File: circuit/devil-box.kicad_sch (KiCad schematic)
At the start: 17 parts, among them M1 Motor_Servo, SW1 SW_Push, T1 BSS83P, T2 BSS83P, T3 BSS83P, T4 BUZ11, T5 BSS83P

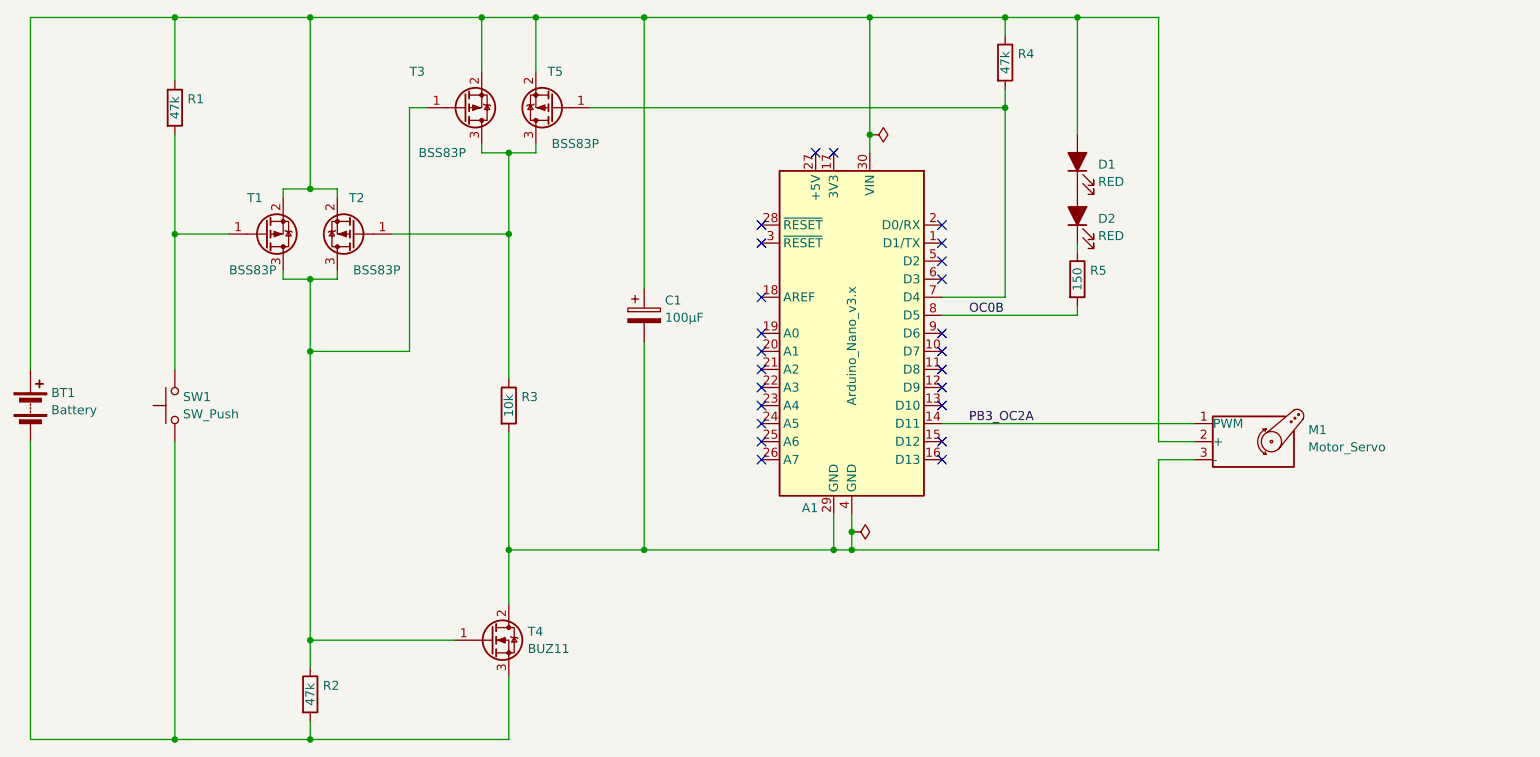
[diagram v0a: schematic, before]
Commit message: add capacitor; changed stop pin D4-A0
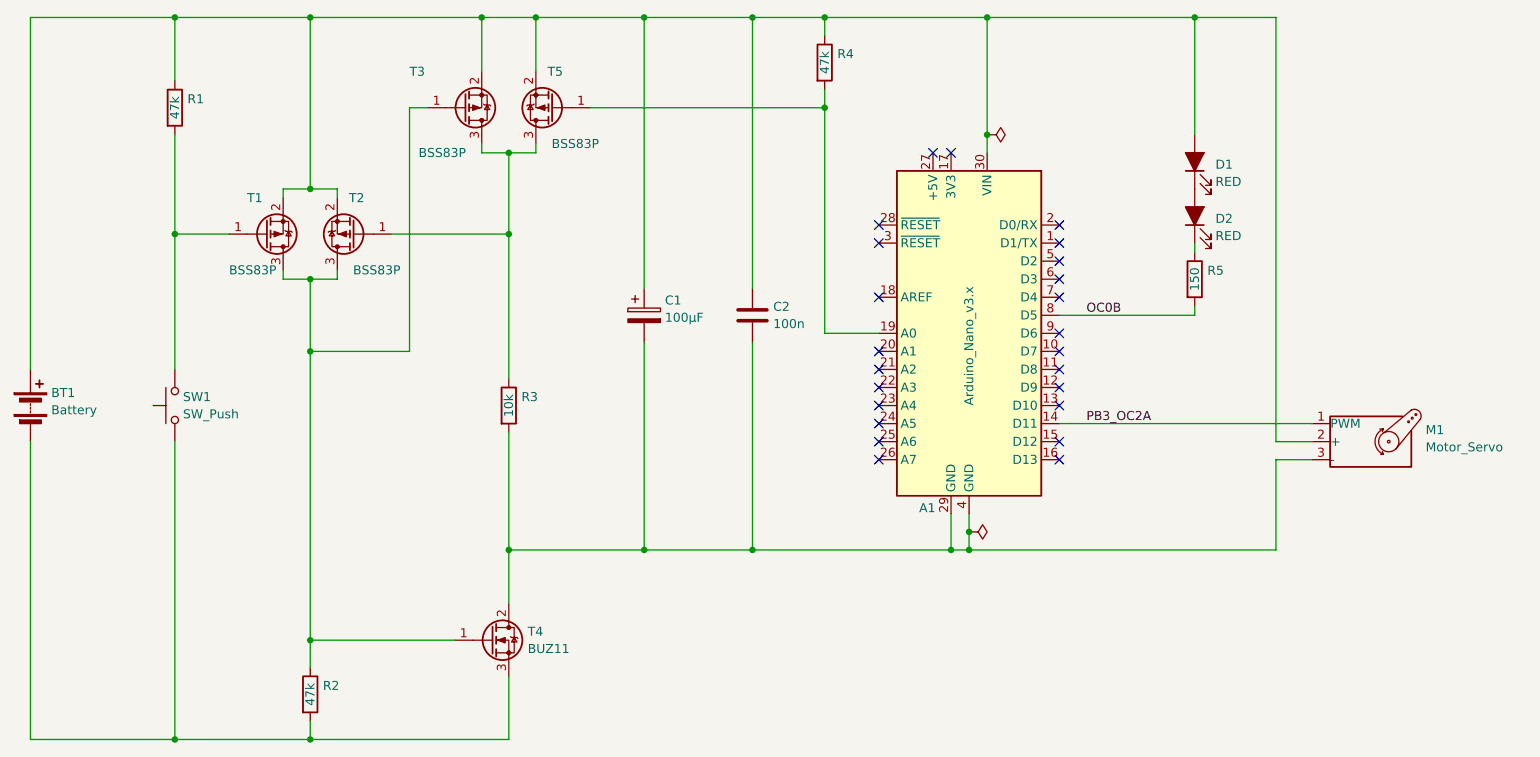
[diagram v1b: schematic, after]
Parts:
- added C2: 100n, symbol Device:C
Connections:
- net at A1.30 (VIN), BT1.1 (+), C1.1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: now also C2.1
- net at A1.29 (GND), A1.4 (GND), C1.2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: now also C2.2
- net at A1.19 (A0): now also R4.2, T5.1 (G)
- now unconnected: A1.7 (D4)
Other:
- title: (none) -> Devil box
- moved on the sheet: A1, D1, D2, M1, R4, R5

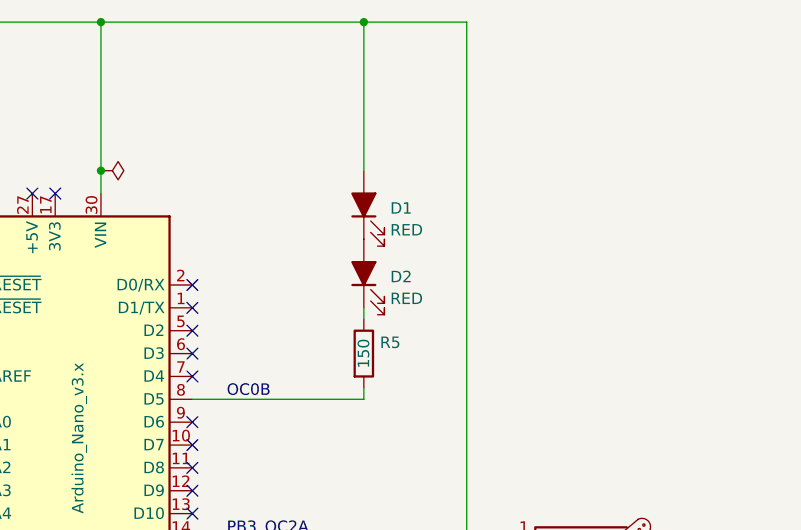
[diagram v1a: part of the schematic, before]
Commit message: footprints assigned, LED series for better implementation
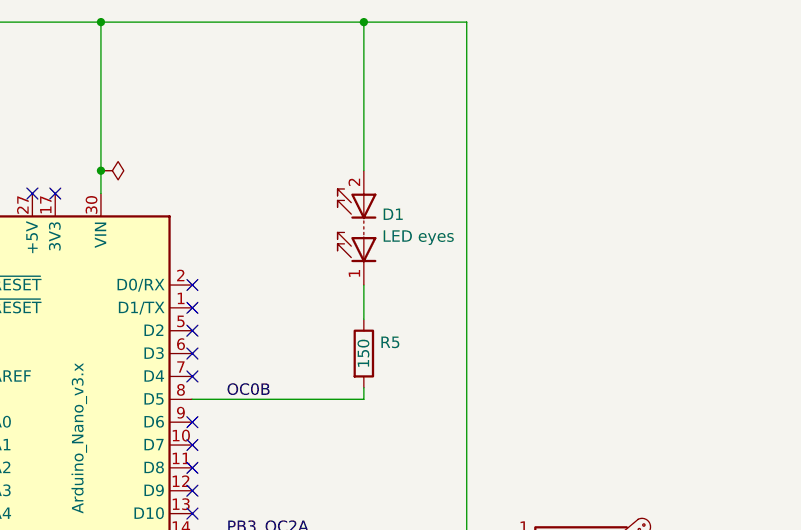
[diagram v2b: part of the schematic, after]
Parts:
- removed D1, D2: RED, Connector_PinHeader_2.54mm:PinHeader_1x02_P2.54mm_Vertical, symbol Device:LED_Filled
- added D1: LED eyes, Connector_PinHeader_2.54mm:PinHeader_1x02_P2.54mm_Vertical, symbol Device:LED_Series
- C2: footprint (none) -> Misi:C_Polstarek_L12mm_W2mm_P5mm
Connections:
- net at A1.30 (VIN), BT1.1 (+), C1.1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: now also D1.2 (A)
- net at R5.1: now also D1.1 (K)
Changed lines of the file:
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@@
 	(wire
 		(pts
-			(xy 228.6 73.66) (xy 228.6 74.93)
+			(xy 228.6 71.12) (xy 228.6 74.93)
 		)
 		(stroke
@@
 	)
 	(symbol
-		(lib_id "Device:LED_Filled")
-		(at 228.6 69.85 90)
-		(unit 1)
-		(exclude_from_sim no)
-		(in_bom yes)
-		(on_board yes)
-		(dnp no)
-		(fields_autoplaced yes)
-		(property "Reference" "D2"
-			(at 231.521 70.2254 90)
-			(effects
-				(font
-					(size 1.27 1.27)
-				)
-				(justify right)
-			)
-		)
-		(property "Value" "RED"
-			(at 231.521 72.6496 90)
-			(effects
-				(font
-					(size 1.27 1.27)
-				)
-				(justify right)
-			)
-		)
-		(property "Footprint" "Connector_PinHeader_2.54mm:PinHeader_1x02_P2.54mm_Vertical"
-			(at 228.6 69.85 0)
-			(effects
-				(font
-					(size 1.27 1.27)
-				)
-				(hide yes)
-			)
-		)
-		(property "Datasheet" "~"
-			(at 228.6 69.85 0)
-			(effects
-				(font
-					(size 1.27 1.27)
-				)
-				(hide yes)
-			)
-		)
-		(property "Description" ""
-			(at 228.6 69.85 0)
-			(effects
-				(font
-					(size 1.27 1.27)
-				)
-				(hide yes)
-			)
-		)
-		(pin "1"
-		)
-		(pin "2"
-		)
-		(instances
-			(project "devil-box"
-				(path "/c6112e97-0a50-4811-b9a7-b9d8fe3a9480"
-					(reference "D2")
-					(unit 1)
-				)
-			)
-		)
-	)
-	(symbol
 		(lib_id "power:PWR_FLAG")
 		(at 196.85 114.3 270)
@@
 			)
 		)
-		(property "Footprint" ""
+		(property "Footprint" "Misi:C_Polstarek_L12mm_W2mm_P5mm"
 			(at 167.3352 87.63 0)
 			(effects
@@
 	)
 	(symbol
-		(lib_id "Device:LED_Filled")
-		(at 228.6 62.23 90)
+		(lib_id "Device:LED_Series")
+		(at 228.6 64.77 90)
 		(unit 1)
 		(exclude_from_sim no)
@@
 		(fields_autoplaced yes)
 		(property "Reference" "D1"
-			(at 231.521 62.6054 90)
+			(at 230.632 63.3038 90)
 			(effects
 				(font
@@
 			)
 		)
-		(property "Value" "RED"
-			(at 231.521 65.0296 90)
+		(property "Value" "LED eyes"
+			(at 230.632 65.7281 90)
 			(effects
 				(font
@@
 		)
 		(property "Footprint" "Connector_PinHeader_2.54mm:PinHeader_1x02_P2.54mm_Vertical"
-			(at 228.6 62.23 0)
+			(at 228.6 67.31 0)
 			(effects
 				(font
@@
 		)
 		(property "Datasheet" "~"
-			(at 228.6 62.23 0)
-			(effects
-				(font
-					(size 1.27 1.27)
-				)
-				(hide yes)
-			)
-		)
-		(property "Description" ""
-			(at 228.6 62.23 0)
+			(at 228.6 67.31 0)
+			(effects
+				(font
+					(size 1.27 1.27)
+				)
+				(hide yes)
+			)
+		)
+		(property "Description" "Several LEDs in series"
+			(at 228.6 64.77 0)
 			(effects
 				(font
@@
 		)
 		(instances
-			(project "devil-box"
+			(project ""
 				(path "/c6112e97-0a50-4811-b9a7-b9d8fe3a9480"
 					(reference "D1")
